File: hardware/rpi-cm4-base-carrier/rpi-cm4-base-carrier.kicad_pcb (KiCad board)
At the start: 4 copper layers, 192.1 x 99.1 mm, 76 parts, among them IC1 KTD2052BEVAA-TR, J1 690-019-298-412, J10 Conn_02x05_Odd_Even, J11 XM7B-0442, J2 DNP, J3 USB4105-GF-A, J4 SM04B-SRSS-TB(LF)(SN), J5 THD-02-R, J6 JT4-1202HL, J7 Micro_SD_Card_Det, J9 690-008-221-904, U1 RT9742SNGV, U2 TPD4EUSB30, U3 TPD4EUSB30, U4 RT9742GGJ5, U5 FSUSB42MUX, U6 USB2514B-I/M2, U7 TPD4EUSB30, U8 AP22653W6, U9 74LVC1G07SE-7, Y1 CX3225CA24000D0HSSCC

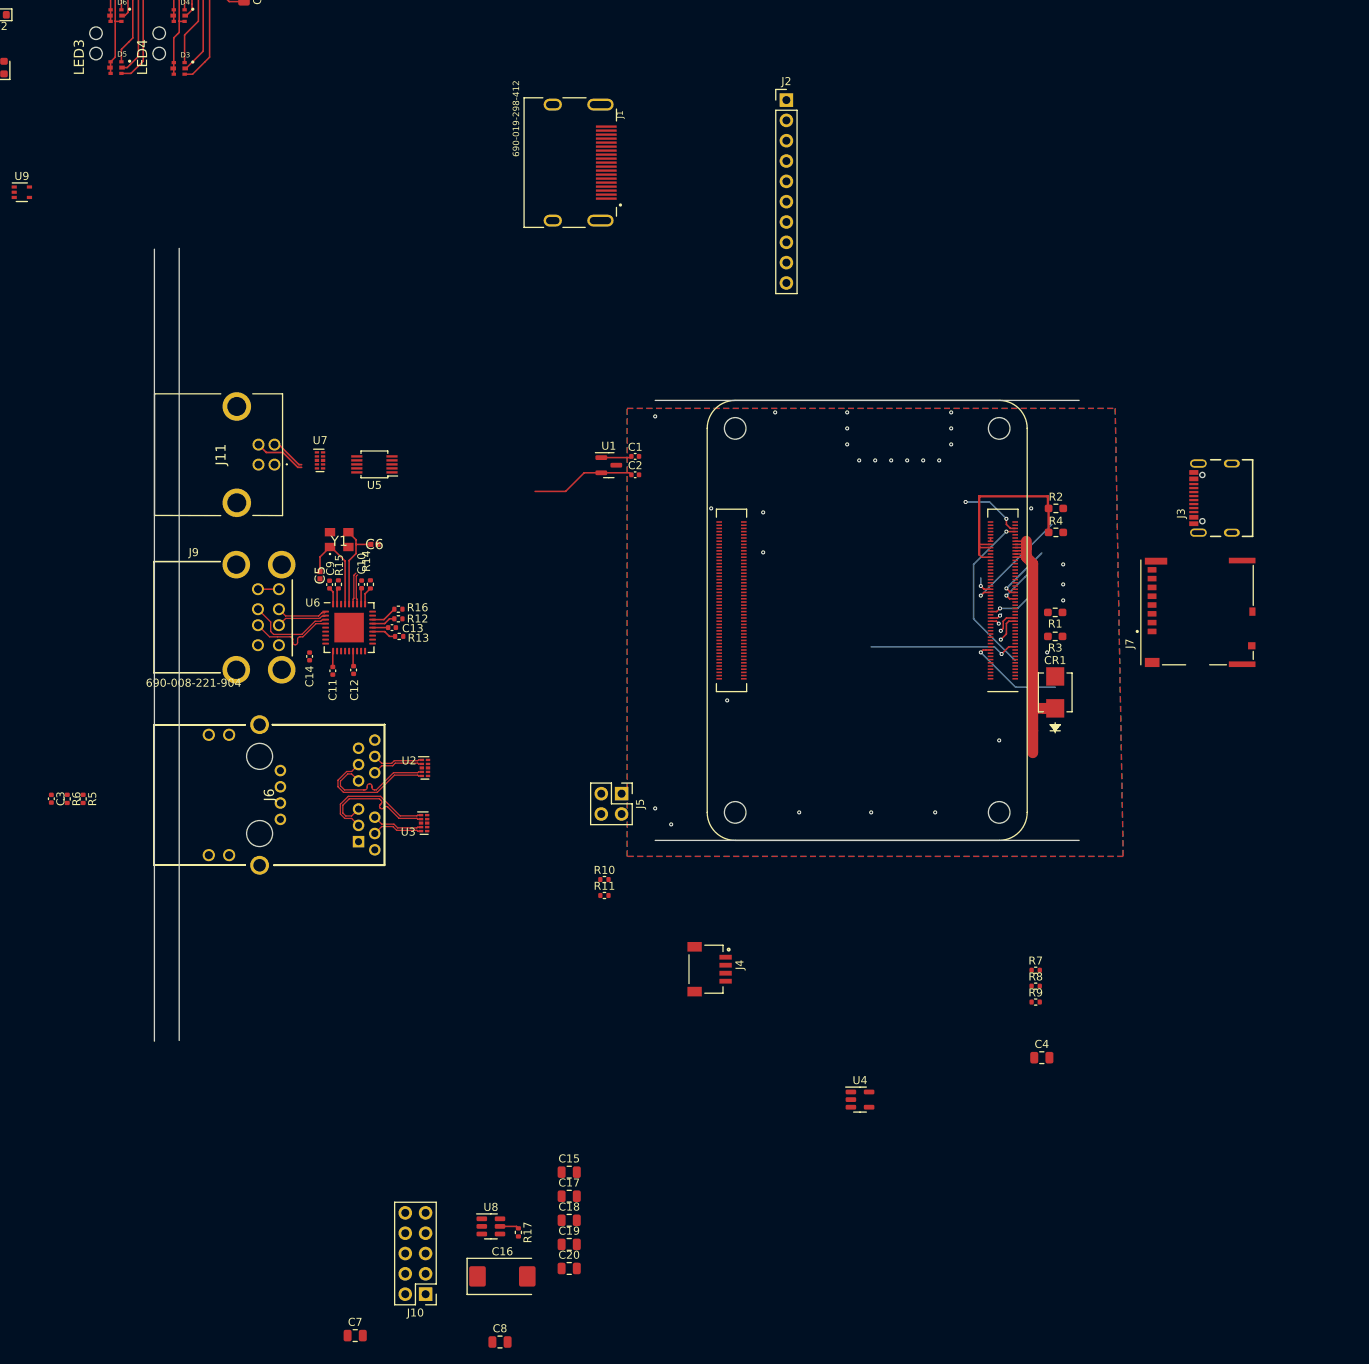
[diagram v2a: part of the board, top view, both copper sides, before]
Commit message: started to route core connectors to CM4, RJ45 annoyingly has the inverse pinout to CM4, need to work out how to uncross tracking sensibly
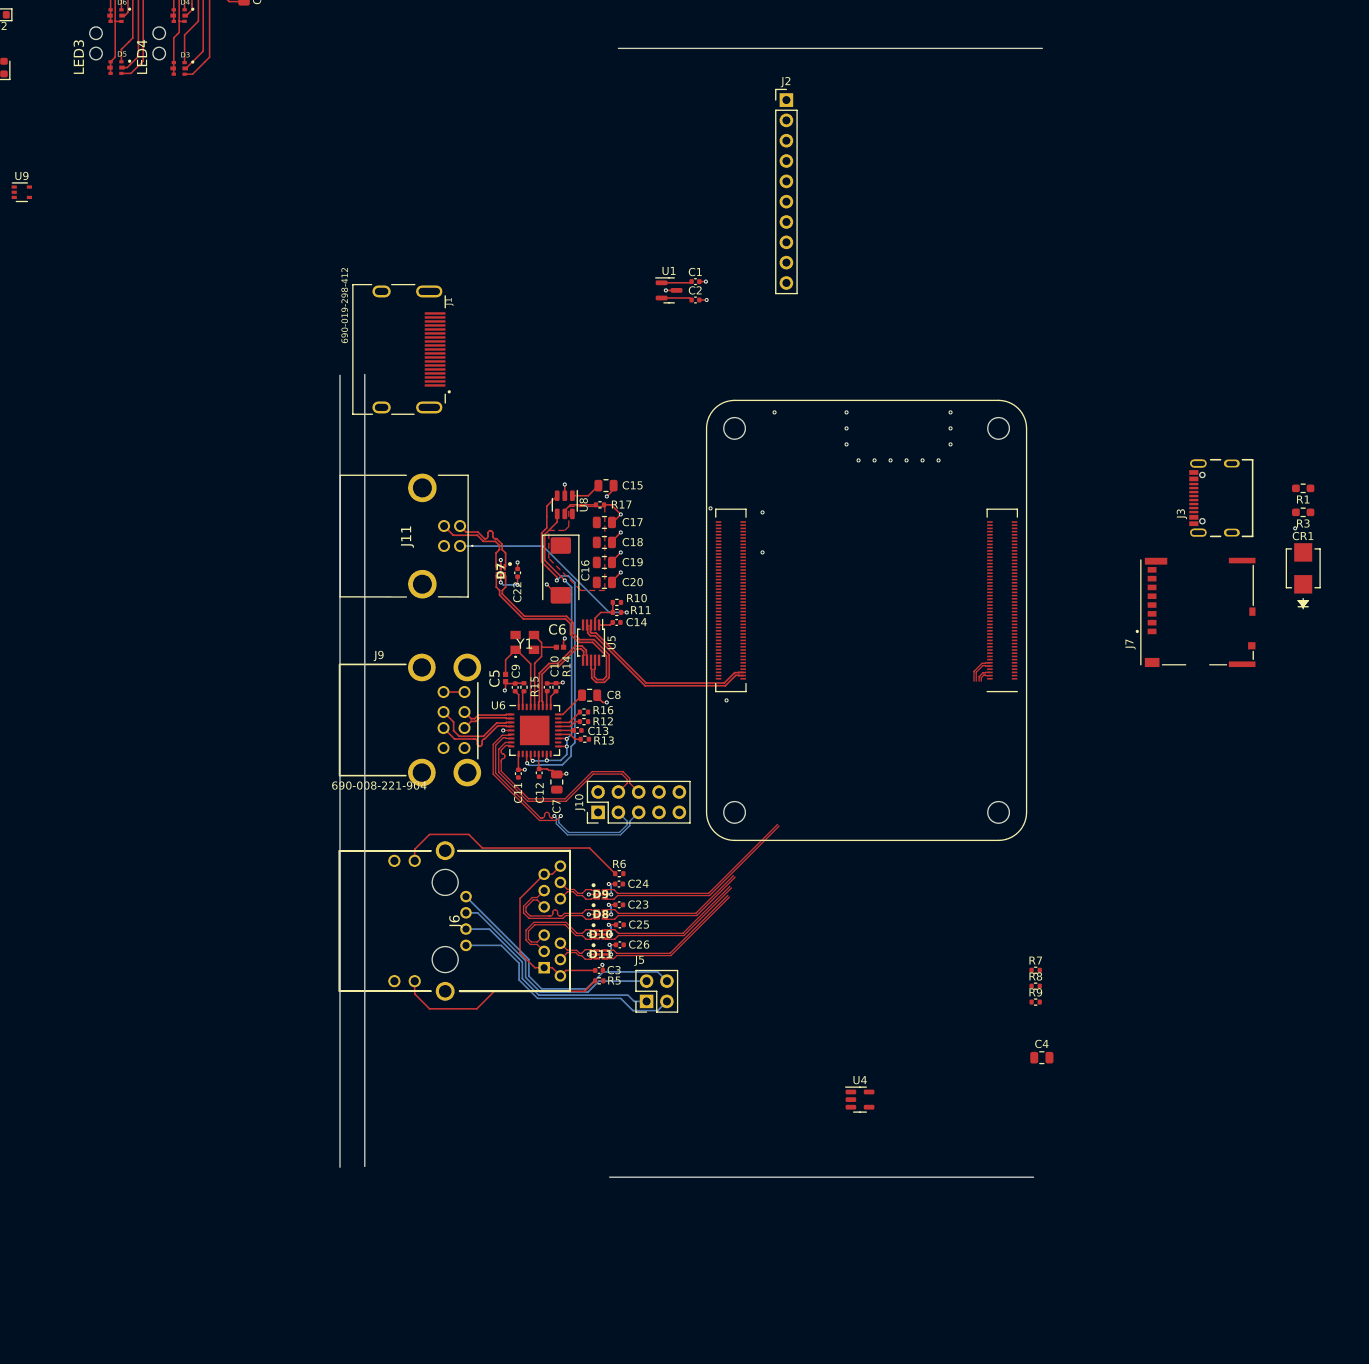
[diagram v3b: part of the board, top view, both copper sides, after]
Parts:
- removed J4: SM04B-SRSS-TB(LF)(SN), SM04B-SRSS-TB_LF__SN_:JST_SM04B-SRSS-TB(LF)(SN)
- removed R2, R4: DNP, Resistor_SMD:R_0603_1608Metric_Pad0.98x0.95mm_HandSolder
- removed U2, U3, U7: TPD4EUSB30, Package_SON:USON-10_2.5x1.0mm_P0.5mm
- added C22: 100n, Capacitor_SMD:C_0402_1005Metric, F.Cu at (102.3, 98.6)
- added C23: 100n, Capacitor_SMD:C_0402_1005Metric, F.Cu at (115.0, 140.1)
- added C24: 100n, Capacitor_SMD:C_0402_1005Metric, F.Cu at (115.0, 137.5)
- added C25: 100n, Capacitor_SMD:C_0402_1005Metric, F.Cu at (115.1, 142.6)
- added C26: 100n, Capacitor_SMD:C_0402_1005Metric, F.Cu at (115.1, 145.1)
- added D10: USBULC6-2M6, SamacSys_Parts:SON50P100X145X60-6N-D, F.Cu at (112.7, 143.8)
- added D11: USBULC6-2M6, SamacSys_Parts:SON50P100X145X60-6N-D, F.Cu at (112.7, 146.3)
- added D7: USBULC6-2M6, SamacSys_Parts:SON50P100X145X60-6N-D, F.Cu at (100.2, 98.4)
- added D8: USBULC6-2M6, SamacSys_Parts:SON50P100X145X60-6N-D, F.Cu at (112.7, 141.3)
- added D9: USBULC6-2M6, SamacSys_Parts:SON50P100X145X60-6N-D, F.Cu at (112.7, 138.8)
- moved R17 91.5 mm to (112.6, 90.1), turned to 0 degrees
- moved U8 90.7 mm to (108.2, 90.1), turned to -90 degrees
- moved C16 88.5 mm to (107.7, 98.3), turned to -90 degrees
- moved C15 85.9 mm to (113.3, 87.7)
- moved C20 85.9 mm to (113.2, 99.8)
- moved C19 85.4 mm to (113.2, 97.3)
- moved C18 84.8 mm to (113.2, 94.8)
- moved C17 84.3 mm to (113.2, 92.3)
- moved C8 81.6 mm to (111.3, 113.9)
- moved C7 73.6 mm to (107.2, 124.7), turned to -90 degrees
- moved C3 71.7 mm to (112.5, 148.3), turned to 0 degrees
- moved R6 69.6 mm to (115.0, 136.2), turned to 0 degrees
- moved R5 68.4 mm to (112.5, 149.6), turned to 0 degrees
- moved J10 64.0 mm to (112.4, 128.5), turned to 90 degrees
- moved C14 38.6 mm to (114.7, 104.8), turned to 0 degrees
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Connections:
- J1 pad 10: /CM4 High Speed/HDMI0_CK_N -> /CM4 High Speed/HDMI0_CK_P
- J1 pad 4: /CM4 High Speed/HDMI0_CK_N -> /CM4 High Speed/HDMI0_D1_P
- J1 pad 6: /CM4 High Speed/HDMI0_CK_N -> /CM4 High Speed/HDMI0_D1_N
- J1 pad 7: /CM4 High Speed/HDMI0_CK_N -> /CM4 High Speed/HDMI0_D0_P
- J1 pad 9: /CM4 High Speed/HDMI0_CK_N -> /CM4 High Speed/HDMI0_D0_N
- Module1 pad 176: /CM4 High Speed/HDMI0_CK_N -> /CM4 High Speed/HDMI0_D1_P
- Module1 pad 178: /CM4 High Speed/HDMI0_CK_N -> /CM4 High Speed/HDMI0_D1_N
- Module1 pad 182: /CM4 High Speed/HDMI0_CK_N -> /CM4 High Speed/HDMI0_D0_P
- Module1 pad 184: /CM4 High Speed/HDMI0_CK_N -> /CM4 High Speed/HDMI0_D0_N
- Module1 pad 188: /CM4 High Speed/HDMI0_CK_N -> /CM4 High Speed/HDMI0_CK_P
- U5 pad 1: unconnected-(U5-VCC-Pad1) -> +3V3
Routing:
- net /CM4 High Speed/USB2-HUB/PWR1: track 0.00 -> 44.2 mm, vias 0 -> 2
- net /CM4 High Speed/USB2-HUB/nOCS1: track 0.00 -> 41.0 mm, vias 0 -> 5
- net +5V: track 42.5 -> 7.59 mm
- net /CM4 High Speed/USB2-HUB/USBD_N: track 4.43 -> 38.3 mm
- net GND: track 4.60 -> 37.2 mm, vias 29 -> 39
- net /magjack/TR3_TAP: track 0.00 -> 32.5 mm
- net /CM4 High Speed/USB2-HUB/USBD_P: track 6.57 -> 37.3 mm
- net /magjack/TR0_TAP: track 0.00 -> 30.2 mm
- net /CM4 High Speed/USB2-HUB/HD3_N: track 0.00 -> 30.0 mm, vias 0 -> 1
- net /CM4 High Speed/USB2-HUB/HD3_P: track 0.00 -> 29.9 mm, vias 0 -> 1
- net Net-(J6-K_GREEN): track 0.00 -> 29.3 mm
- net /magjack/TR2_TAP: track 0.00 -> 28.5 mm
- net /magjack/TR1_TAP: track 0.00 -> 27.5 mm
- net Net-(J6-K_YELLOW): track 0.00 -> 26.4 mm
- net /CM4 High Speed/USB2-HUB/HD4_N: track 0.00 -> 26.1 mm
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- added copper zone on F.Cu, net /CM4 High Speed/USB2-HUB/VBUS
- removed copper zone on B.Cu, net GND
- removed copper zone on F.Cu, net GND
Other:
- board size 192.1 x 99.1 mm -> 168.9 x 141.1 mm

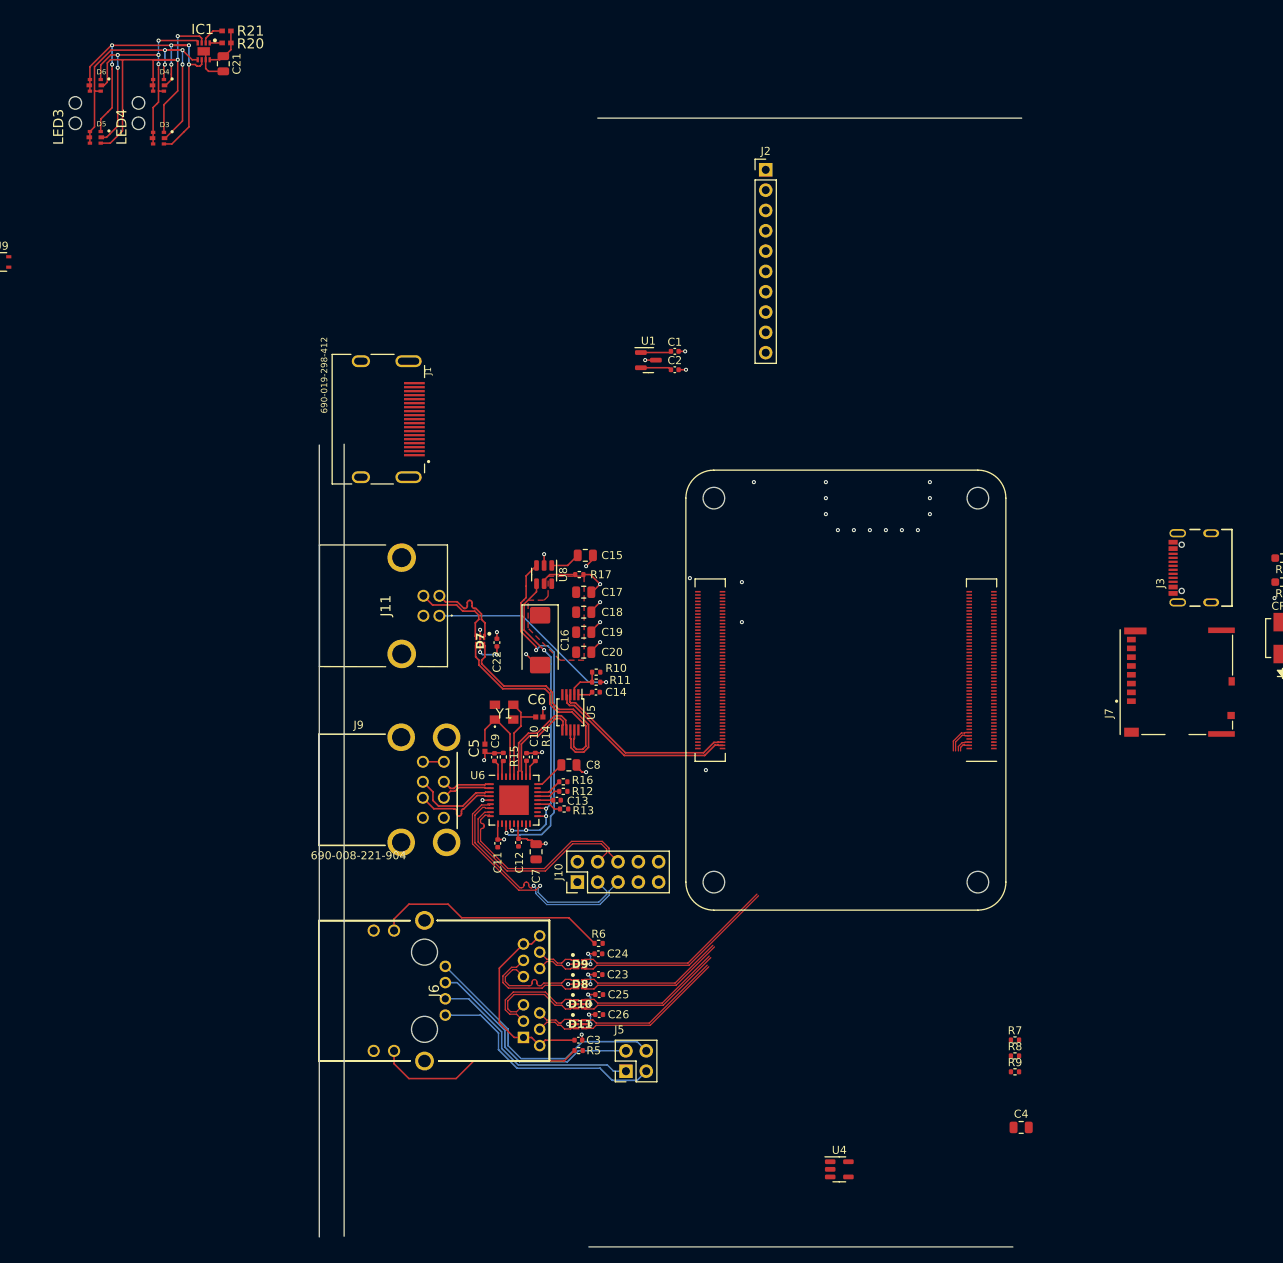
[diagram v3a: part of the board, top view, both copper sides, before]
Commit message: most diff pairs routed, forgot about intra-pair spacing
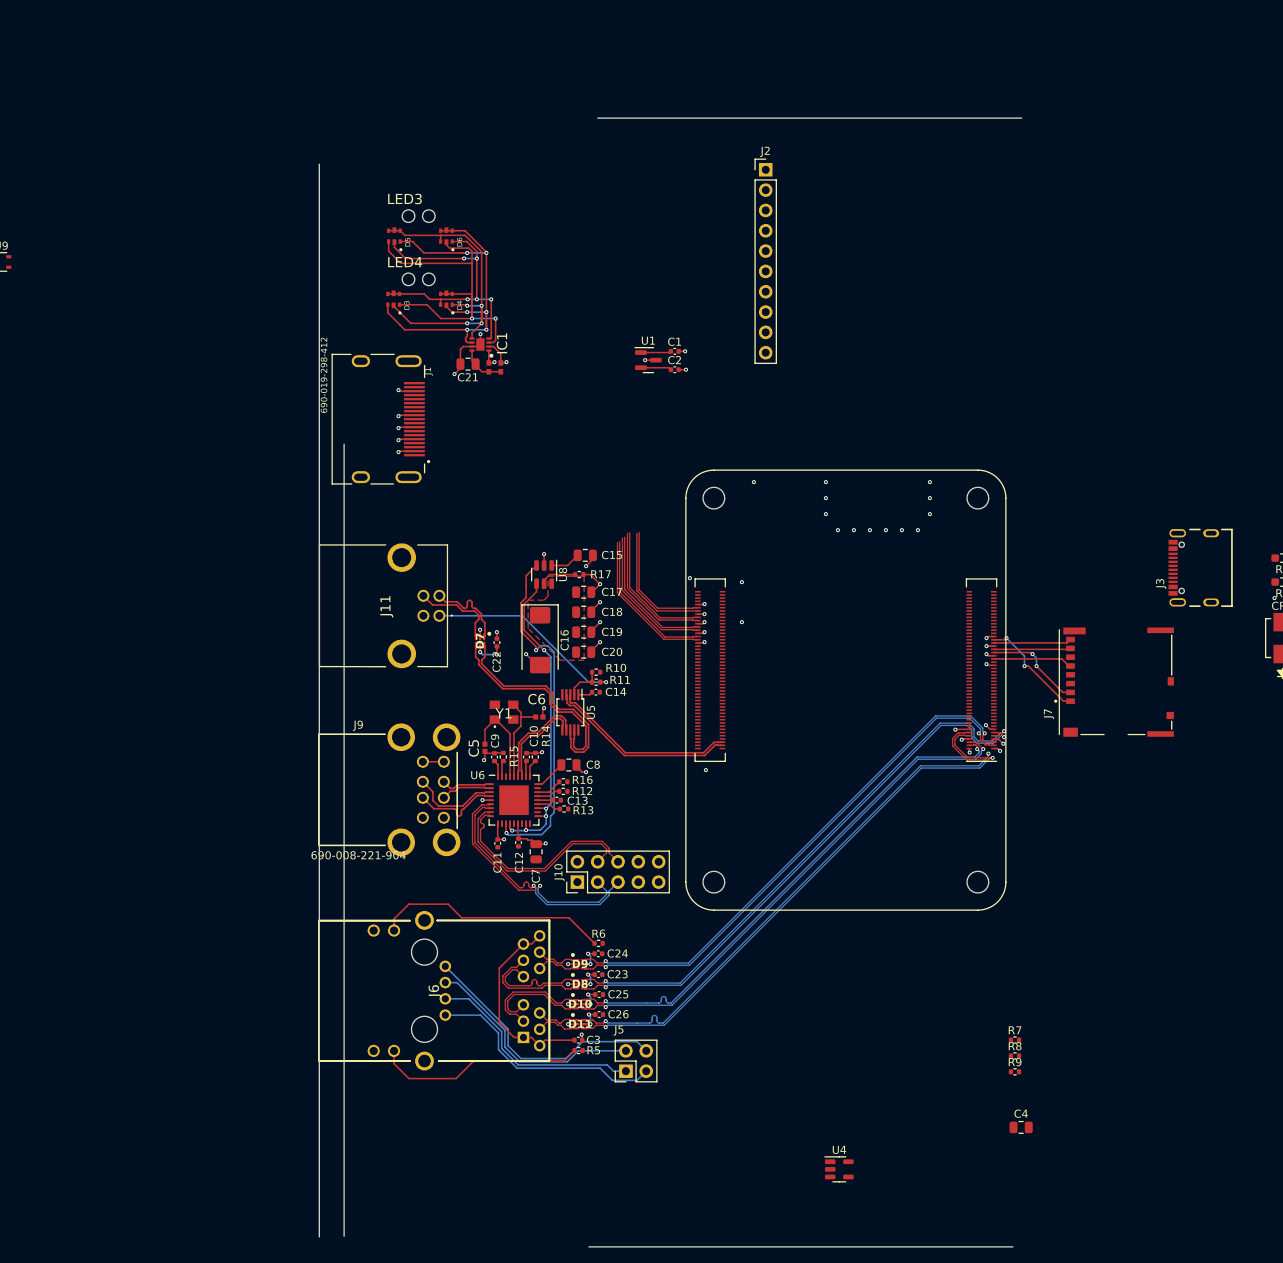
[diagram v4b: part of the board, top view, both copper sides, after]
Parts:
- moved R21 54.3 mm to (102.8, 64.2), turned to -90 degrees
- moved R20 52.1 mm to (101.3, 64.2), turned to -90 degrees
- moved IC1 50.4 mm to (100.2, 61.3), turned to 180 degrees
- moved C21 48.4 mm to (98.7, 63.8), turned to 180 degrees
- moved D6 47.8 mm to (96.0, 47.8), turned to -90 degrees
- moved D4 44.8 mm to (96.0, 55.6), turned to -90 degrees
- moved D5 39.4 mm to (89.5, 47.8), turned to -90 degrees
- moved D3 35.6 mm to (89.4, 55.6), turned to -90 degrees
- moved LED3 29.2 mm to (79.6, 46.0), turned to -90 degrees
- moved LED4 23.0 mm to (79.6, 53.9), turned to -90 degrees
- moved J7 7.61 mm to (179.6, 103.5)
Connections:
- D7 pad 3: /CM4 High Speed/USB2-HUB/USBD_P -> unconnected-(D7-D--Pad3)
- D7 pad 4: /CM4 High Speed/USB2-HUB/USBD_P -> GND
- J1 pad 1: /CM4 High Speed/HDMI0_CK_N -> /CM4 High Speed/HDMI0_D2_P
- J1 pad 3: /CM4 High Speed/HDMI0_CK_N -> /CM4 High Speed/HDMI0_D2_N
- J11 pad 3: /CM4 High Speed/USB2-HUB/USBD_P -> GND
- Module1 pad 170: /CM4 High Speed/HDMI0_CK_N -> /CM4 High Speed/HDMI0_D2_P
- Module1 pad 172: /CM4 High Speed/HDMI0_CK_N -> /CM4 High Speed/HDMI0_D2_N
- U5 pad 9: /CM4 High Speed/USB2-HUB/USBD_P -> GND
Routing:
- net GND: track 37.2 -> 91.7 mm, vias 39 -> 61
- net /CM4 GPIO/TRD0_N: track 27.1 -> 79.7 mm, vias 0 -> 2
- net /CM4 GPIO/TRD0_P: track 27.7 -> 79.7 mm, vias 0 -> 2
- net /CM4 GPIO/TRD2_P: track 32.3 -> 83.8 mm, vias 0 -> 2
- net /CM4 GPIO/TRD2_N: track 32.5 -> 83.8 mm, vias 0 -> 2
- net /CM4 GPIO/TRD1_P: track 34.1 -> 80.0 mm, vias 0 -> 2
- net /CM4 GPIO/TRD1_N: track 33.8 -> 79.0 mm, vias 0 -> 2
- net /CM4 GPIO/TRD3_N: track 31.0 -> 72.5 mm, vias 0 -> 2
- net /CM4 GPIO/TRD3_P: track 31.2 -> 72.5 mm, vias 0 -> 2
- net /CM4 High Speed/USB2-HUB/USBD_P: track 37.3 -> 10.9 mm
- net /CM4 High Speed/HDMI0_D2_P: track 0.00 -> 18.7 mm
- net /CM4 High Speed/HDMI0_D2_N: track 0.00 -> 18.4 mm
- net /CM4 High Speed/HDMI0_D1_P: track 0.00 -> 18.0 mm
- net /CM4 High Speed/HDMI0_D1_N: track 0.00 -> 17.7 mm
- net /CM4 High Speed/HDMI0_D0_P: track 0.00 -> 17.3 mm
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- added copper zone on In2.Cu, net GND
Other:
- outline, holes or cut-outs redrawn
